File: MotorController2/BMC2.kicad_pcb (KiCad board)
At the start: 2 copper layers, 96 x 56 mm, 131 parts, among them P1 Sensor, P10 GND, P11 I2C, P12 CAN, P2 CAN, P3 DATA, P4 USB_OTG, P5 PhaseA, P6 PhaseB, P7 PhaseC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

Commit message: Tweaks to PCB.
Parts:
- moved W7 0.70 mm to (193.2, 69.8)
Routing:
- net GND: track 735.2 -> 889.5 mm, vias 86 -> 108

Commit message: BMCV2.1 updates.
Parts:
- removed D9: LED, LEDs:LED_0805
- removed P11: I2C, Pin_Headers:Pin_Header_Straight_1x04
- removed R15, R18, R19: 10K, Resistors_SMD:R_0805_HandSoldering
- removed R34: 100R, Resistors_SMD:R_0805_HandSoldering
- removed W11: GND, Measurement_Points:Measurement_Point_Round-SMD-Pad_Big
- removed W14: PB12, Measurement_Points:Measurement_Point_Round-SMD-Pad_Small
- added C45: 1nF 50V, Capacitors_SMD:C_0805_HandSoldering, F.Cu at (142.3, 98.7)
- added C46: 1nF 50V, Capacitors_SMD:C_0805_HandSoldering, F.Cu at (136.7, 93.5)
- added C47: 1nF 50V, Capacitors_SMD:C_0805_HandSoldering, F.Cu at (139.0, 93.6)
- added C48: 100pF 50V, Capacitors_SMD:C_0805_HandSoldering, F.Cu at (175.0, 98.6)
- added C49: 100pF 50V, Capacitors_SMD:C_0805_HandSoldering, F.Cu at (175.0, 100.5)
- added C50: 100pF 50V, Capacitors_SMD:C_0805_HandSoldering, F.Cu at (175.0, 102.4)
- added U6: MIC2009A-1YM6TR, TO_SOT_Packages_SMD:SOT-23-6, F.Cu at (139.7, 88.5)
- added U7: MIC2009A-1YM6TR, TO_SOT_Packages_SMD:SOT-23-6, F.Cu at (142.5, 102.8)
- added W6: GLC, Measurement_Points:Measurement_Point_Round-SMD-Pad_Small, F.Cu at (212.1, 109.2)
- added W9: GHC, Measurement_Points:Measurement_Point_Round-SMD-Pad_Small, F.Cu at (211.8, 94.8)
- C1, C44: value 0.1uf (6V min) -> 0.1uF 50V
- C10, C11, C12, C7: value 100nf -> 0.1uF 50V
- C13: value 10nf -> 0.1uF 50V
- C14: value 1uf -> 1uF 50V
- C15, C16, C25: value 0.1uF 5V -> 0.1uF 50V
- C17: value 1uF 4V -> 1uF 50V
- C18: value 1uf 16V -> 1uF 100V
- C19, C20: value 1uf 6.3V -> 1uF 50V
- C2: value 0.1uF -> 0.1uF 50V
- C21: value 0.1uF 5V -> 10nF 50V
- C22: value 0.047uf 90V -> 47nF 200V
- C23: value 0.047uf 45v -> 47nF 200V
- C24, C26: value 1nF 5V -> 1nF 50V
- C27: value 2.2uf 16V -> 2.2uF 50V
- C28: value 4.7uF 45V -> 4.7uF 100V
- C29: value 1nf 5V -> 1nF 50V
- C3, C4: value 2.2uf -> 2.2uF 50V
- C30, C31, C32: value 1uF 50V -> 1uF 100V
- C36, C39: value 220nF 60V -> 220nF 100V
- C37: value 100uF 60V -> 100uF 63V
- C38: value 22nF 6V -> 22nF 50V
- C40: value 220nF 6V -> 220nF 25V
- C41: value 100uF 6V -> 100uF 6.3V
- C42: value 220nF 6V -> 220nF 100V
- C43: value 1uF 4V min -> 1uF 50V
- C8: value 4.7uf -> 4.7uF 25V
- C9: value 100nf 5V -> 0.1uF 50V
- D1: value 10V -> 60V 2A
- D3: value RED LED -> YELLOW
- D5: value 60V 2A -> 60V 2A
- D6: value 50V -> 60V 2A
- D7: value 5.4V -> 5.6V
- R13: value 10 -> 10R
- R14: value 10K -> 1K
- R2: value 1k -> 300R
- R3, R8: value 1k -> 1K
- R7: value 10k -> 10K
- TH1: value THERMISTOR -> NTC 10K
- moved R3 42.8 mm to (180.6, 98.2)
- moved R8 38.2 mm to (180.6, 100.3), turned to 180 degrees
- moved R2 15.9 mm to (142.5, 107.2), turned to 90 degrees
- moved C25 11.5 mm to (178.8, 108.5), turned to 180 degrees
- moved R14 6.30 mm to (180.6, 102.5), turned to 180 degrees
- moved W5 4.49 mm to (184.5, 102.7)
- moved W4 4.38 mm to (184.4, 100.4)
- moved R23 4.29 mm to (180.6, 105.6)
- moved R1 2.89 mm to (136.4, 87.0), turned to 270 degrees
- moved R20 2.86 mm to (210.0, 58.9)
- moved R7 1.92 mm to (137.6, 106.1)
- moved W12 1.83 mm to (159.7, 63.5)
- moved C2 1.75 mm to (137.6, 108.2)
- moved C15 1.71 mm to (175.1, 104.5), turned to 180 degrees
- moved C3 1.38 mm to (171.1, 99.9)
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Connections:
- C2 pad 1: Net-(C2-Pad1) -> /Controller/Temp
- P1 pad 1: Net-(C2-Pad1) -> /Controller/Temp
- P1 pad 5: Net-(P1-Pad5) -> /Controller/EndStop1
- P1 pad 6: Net-(P1-Pad6) -> /Controller/EndStop2
- P1 pad 7: Net-(P1-Pad7) -> /Controller/Index
- P1 pad 8: +3V3 -> Net-(P1-Pad8)
- P3 pad 4: +5V -> Net-(P3-Pad4)
- R1 pad 1: /Controller/Index -> GND
- R1 pad 2: Net-(P1-Pad7) -> Net-(R1-Pad2)
- R14 pad 1: +3V3 -> Net-(R14-Pad1)
- R14 pad 2: Net-(C15-Pad1) -> /Controller/ISenseC
- R2 pad 1: /Controller/EndStop2 -> GND
- R2 pad 2: Net-(P1-Pad6) -> Net-(R2-Pad2)
- R3 pad 1: /Controller/EndStop1 -> Net-(R3-Pad1)
- R3 pad 2: Net-(P1-Pad5) -> /Controller/ISenseA
- R7 pad 1: Net-(C2-Pad1) -> /Controller/Temp
- R8 pad 1: /Controller/Temp -> Net-(R8-Pad1)
- R8 pad 2: Net-(C2-Pad1) -> /Controller/ISenseB
- U2 pad 23: Net-(U2-Pad23) -> /Controller/FanCtrl
- U2 pad 29: /Controller/I2C_SCL -> /Controller/SENSOR_PWR_FAULT
- U2 pad 30: /Controller/I2C_SDA -> /Controller/FAN_FAULT
- U2 pad 33: Net-(U2-Pad33) -> /Controller/SensorPwrCtrl
- U2 pad 61: /Controller/CAN_TX -> /Controller/CAN_RX
- U2 pad 62: /Controller/CAN_RX -> /Controller/CAN_TX
- U3 pad 16: /Controller/ISenseA -> Net-(R3-Pad1)
- U3 pad 17: /Controller/ISenseB -> Net-(R8-Pad1)
- U3 pad 18: /Controller/ISenseC -> Net-(R14-Pad1)
- W3 pad 1: /Controller/ISenseA -> Net-(R3-Pad1)
- W4 pad 1: /Controller/ISenseB -> Net-(R8-Pad1)
- W5 pad 1: /Controller/ISenseC -> Net-(R14-Pad1)
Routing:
- net /Controller/SENSOR_PWR_FAULT: track 0.00 -> 41.4 mm, vias 0 -> 2
- net /Controller/FanCtrl: track 0.00 -> 36.4 mm
- net /Controller/SensorPwrCtrl: track 0.00 -> 34.7 mm, vias 0 -> 2
- net GND: track 889.5 -> 923.4 mm, vias 108 -> 106
- net /Controller/FAN_FAULT: track 0.00 -> 32.2 mm, vias 0 -> 2
- net /Controller/I2C_SCL: track 26.3 -> 0.00 mm, vias 2 -> 0
- net /Controller/I2C_SDA: track 19.0 -> 0.00 mm
- net Net-(R14-Pad1): track 0.00 -> 15.5 mm
- net /Controller/Temp: track 24.1 -> 39.0 mm
- net Net-(C2-Pad1): track 13.9 -> 0.00 mm
- net Net-(R8-Pad1): track 0.00 -> 12.6 mm
- net /Controller/Index: track 34.5 -> 46.8 mm
- net /Controller/ISenseB: track 30.3 -> 19.4 mm
- net /Controller/ISenseC: track 32.1 -> 21.3 mm
- net Net-(R3-Pad1): track 0.00 -> 10.6 mm
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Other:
- board text added: "BMC V2.1"
- board text removed: "BMC V2.0"

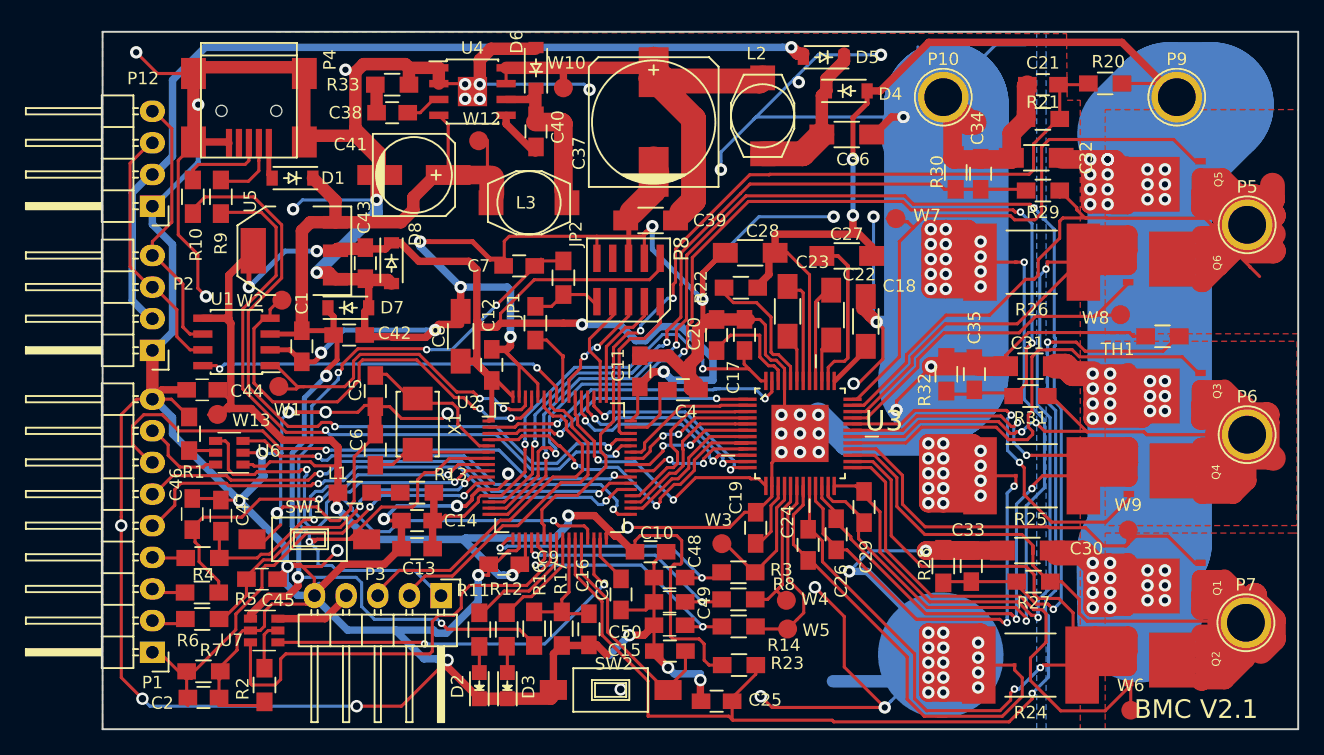
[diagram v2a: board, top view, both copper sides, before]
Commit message: Add power off option.
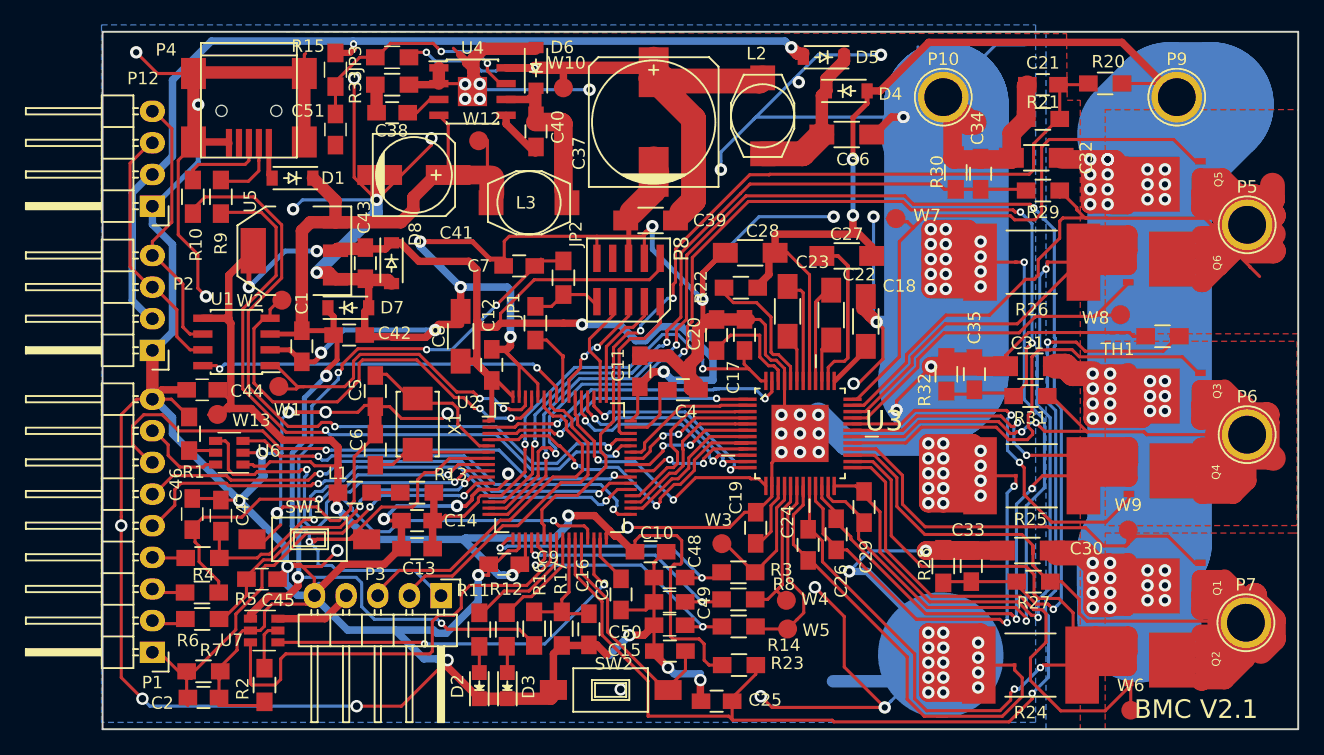
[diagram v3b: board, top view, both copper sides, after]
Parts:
- added C51: 0.1uF 100V, Capacitors_SMD:C_0805_HandSoldering, F.Cu at (148.2, 62.6)
- added JP3: Jumper_NO_Small, Resistors_SMD:R_0805_HandSoldering, F.Cu at (152.8, 56.8)
- added R15: 10k, Resistors_SMD:R_0805_HandSoldering, F.Cu at (148.2, 57.8)
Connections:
- U4 pad 7: Net-(C37-Pad1) -> Net-(C51-Pad1)
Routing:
- net Net-(C51-Pad1): track 0.00 -> 19.7 mm, vias 0 -> 2
- net Net-(C37-Pad1): track 44.2 -> 53.5 mm, vias 0 -> 2
- net GND: track 923.4 -> 920.5 mm
- net +8V: track 73.5 -> 76.2 mm, vias 1 -> 2
- net (no net): vias 0 -> 1

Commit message: Board layouts as ordered.
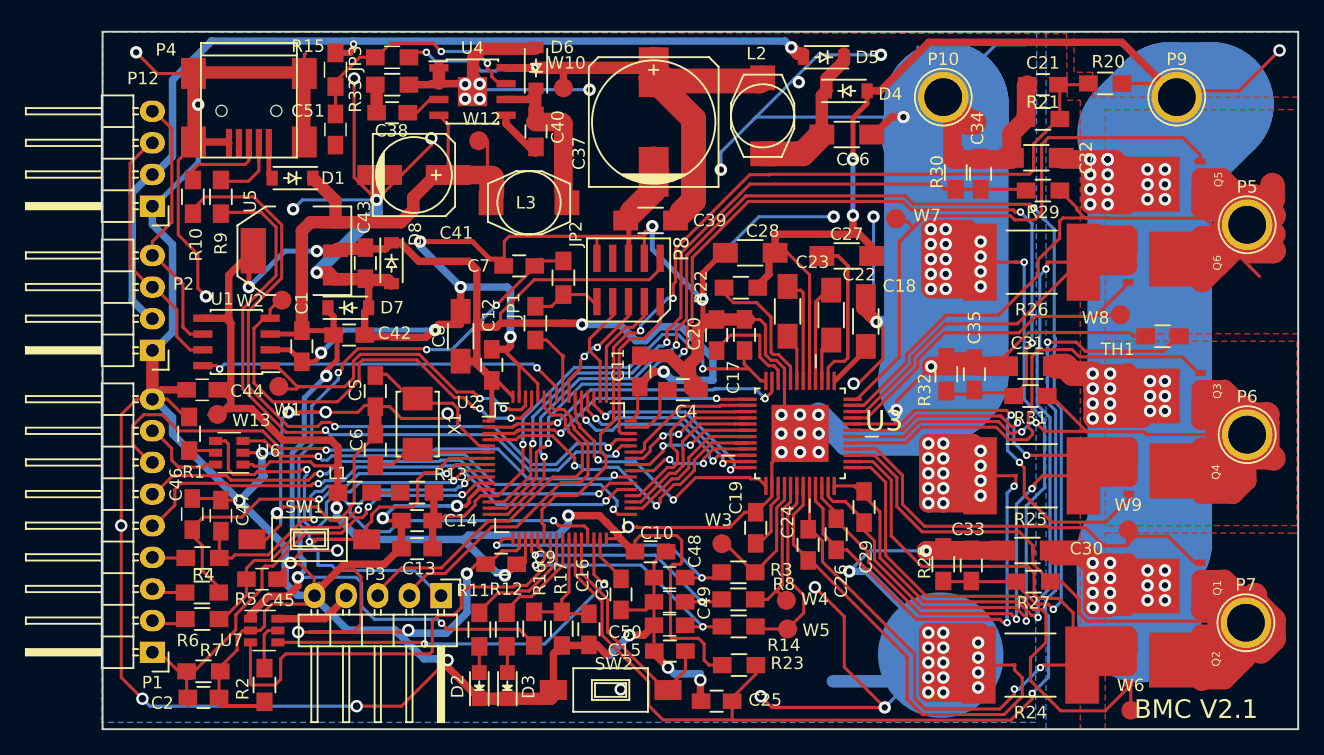
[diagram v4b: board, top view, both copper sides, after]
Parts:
- moved C9 0.25 mm to (161.5, 97.5)
- moved R28 0.15 mm to (197.0, 97.5)
- moved C33 0.05 mm to (199.2, 97.6)
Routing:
- net GND: track 920.5 -> 935.8 mm, vias 106 -> 107
- net +36V: track 240.4 -> 250.2 mm, vias 46 -> 47
- net /Controller/VSenseB: track 82.6 -> 81.0 mm
- net Net-(C29-Pad1): track 53.0 -> 54.2 mm
- net Net-(Q5-Pad4): track 48.5 -> 49.4 mm
- net /Controller/TempDrv: track 95.8 -> 95.1 mm
- added copper zone on F.Cu, net +36V

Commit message: Add some annotations.
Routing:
- net GND: track 935.8 -> 943.5 mm, vias 107 -> 108
- net (no net): vias 1 -> 0
